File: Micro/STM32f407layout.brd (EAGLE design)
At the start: 100 x 80 mm, 44 parts, among them Q1 ASF, T3 FDN340P, T4 AP1117_LIN_REG

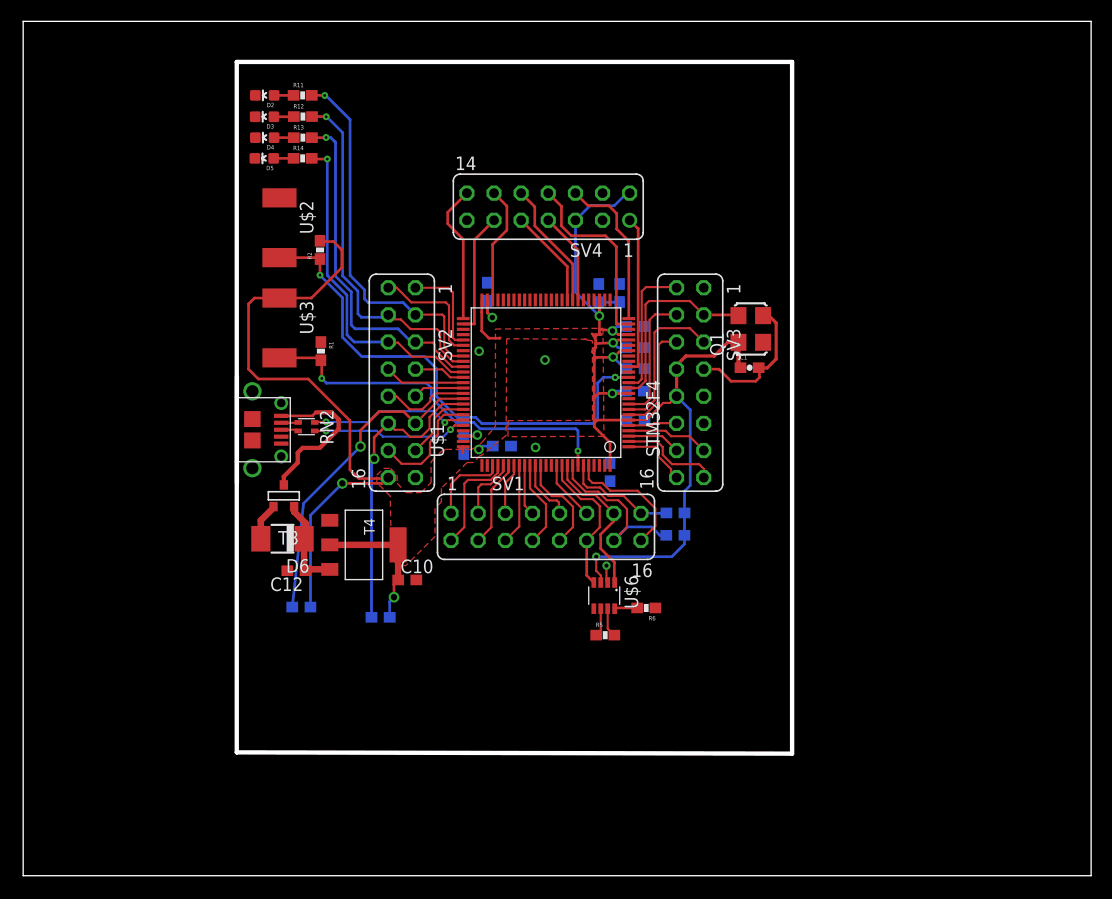
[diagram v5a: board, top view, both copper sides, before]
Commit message: Holiday Update 1
Connected extra capacitors, changed PC0 to GND for now, May route to
better pinout later. Added GND planes made sure no unrouted
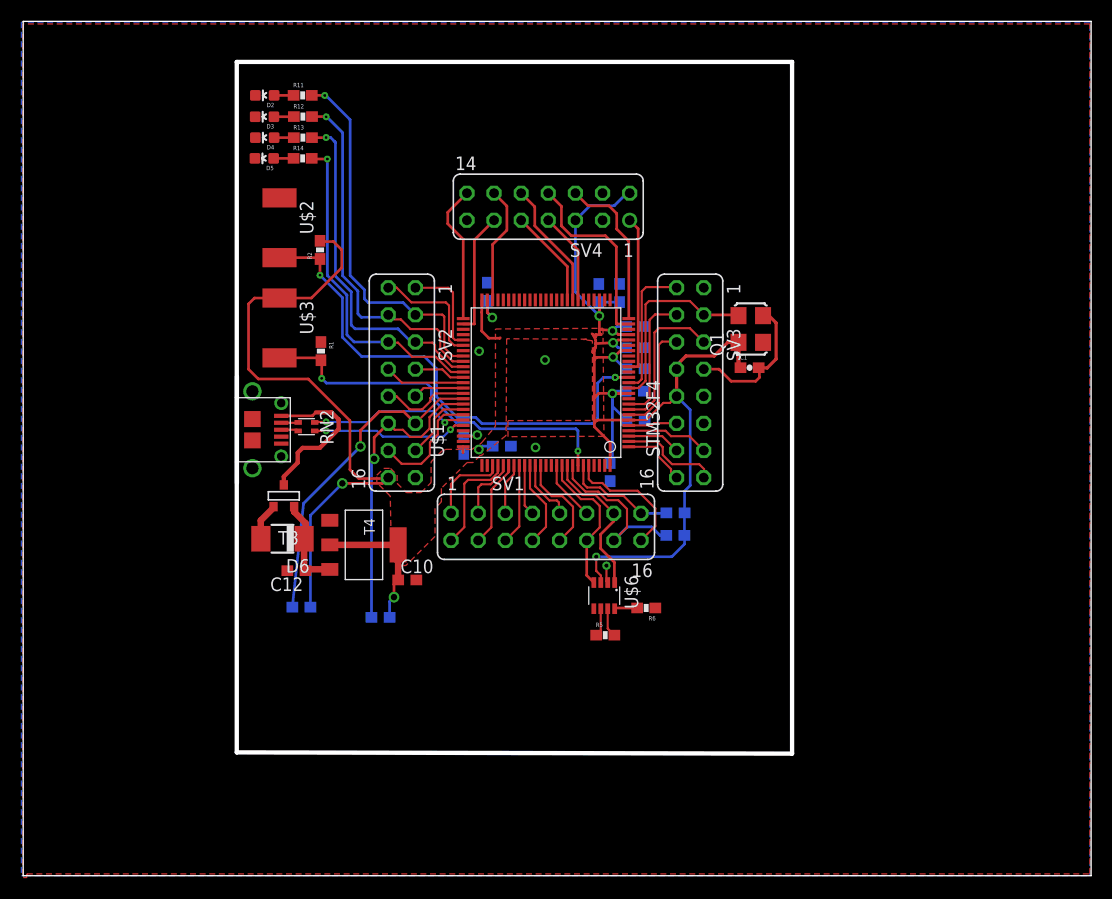
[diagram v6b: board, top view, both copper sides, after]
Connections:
- net GND: now also SV3.1
- net PC0: no longer SV3.1
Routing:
- net +3V3: track 184.5 -> 194.2 mm
- added copper zone on layer 1, net GND
- added copper zone on layer 16, net GND
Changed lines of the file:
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@@
 <layer number="27" name="tValues" color="7" fill="1" visible="yes" active="yes"/>
 <layer number="28" name="bValues" color="7" fill="1" visible="yes" active="yes"/>
-<layer number="29" name="tStop" color="7" fill="3" visible="no" active="yes"/>
-<layer number="30" name="bStop" color="7" fill="6" visible="no" active="yes"/>
+<layer number="29" name="tStop" color="7" fill="3" visible="yes" active="yes"/>
+<layer number="30" name="bStop" color="7" fill="6" visible="yes" active="yes"/>
 <layer number="31" name="tCream" color="7" fill="4" visible="no" active="yes"/>
 <layer number="32" name="bCream" color="7" fill="5" visible="no" active="yes"/>
-<layer number="33" name="tFinish" color="6" fill="3" visible="no" active="yes"/>
-<layer number="34" name="bFinish" color="6" fill="6" visible="no" active="yes"/>
+<layer number="33" name="tFinish" color="6" fill="3" visible="yes" active="yes"/>
+<layer number="34" name="bFinish" color="6" fill="6" visible="yes" active="yes"/>
 <layer number="35" name="tGlue" color="7" fill="4" visible="no" active="yes"/>
 <layer number="36" name="bGlue" color="7" fill="5" visible="no" active="yes"/>
-<layer number="37" name="tTest" color="7" fill="1" visible="no" active="yes"/>
-<layer number="38" name="bTest" color="7" fill="1" visible="no" active="yes"/>
+<layer number="37" name="tTest" color="7" fill="1" visible="yes" active="yes"/>
+<layer number="38" name="bTest" color="7" fill="1" visible="yes" active="yes"/>
 <layer number="39" name="tKeepout" color="4" fill="11" visible="yes" active="yes"/>
 <layer number="40" name="bKeepout" color="1" fill="11" visible="yes" active="yes"/>
@@
 <layer number="42" name="bRestrict" color="1" fill="10" visible="yes" active="yes"/>
 <layer number="43" name="vRestrict" color="2" fill="10" visible="yes" active="yes"/>
-<layer number="44" name="Drills" color="7" fill="1" visible="no" active="yes"/>
-<layer number="45" name="Holes" color="7" fill="1" visible="no" active="yes"/>
-<layer number="46" name="Milling" color="3" fill="1" visible="no" active="yes"/>
-<layer number="47" name="Measures" color="7" fill="1" visible="no" active="yes"/>
+<layer number="44" name="Drills" color="7" fill="1" visible="yes" active="yes"/>
+<layer number="45" name="Holes" color="7" fill="1" visible="yes" active="yes"/>
+<layer number="46" name="Milling" color="3" fill="1" visible="yes" active="yes"/>
+<layer number="47" name="Measures" color="7" fill="1" visible="yes" active="yes"/>
 <layer number="48" name="Document" color="7" fill="1" visible="yes" active="yes"/>
 <layer number="49" name="Reference" color="7" fill="1" visible="yes" active="yes"/>
@@
 <contactref element="SV4" pad="3"/>
 <contactref element="SV4" pad="4"/>
-<wire x1="54.2501375" y1="61.373125" x2="54.2501375" y2="63.913125" width="0" layer="19" extent="1-1"/>
-<wire x1="53.8994875" y1="55.405290625" x2="54.2501375" y2="61.373125" width="0" layer="19" extent="16-16"/>
-<wire x1="54.457" y1="53.915" x2="53.8994875" y2="55.405290625" width="0" layer="19" extent="1-16"/>
-<wire x1="55.845025" y1="55.412146875" x2="53.8994875" y2="55.405290625" width="0" layer="19" extent="16-16"/>
-<wire x1="58.162153125" y1="51.4214625" x2="54.457" y2="53.915" width="0" layer="19" extent="1-16"/>
-<wire x1="58.15608125" y1="49.43988125" x2="58.162153125" y2="51.4214625" width="0" layer="19" extent="16-16"/>
+<polygon width="0.4064" layer="16">
+<vertex x="0.170153125" y="0"/>
+<vertex x="99.885346875" y="0"/>
+<vertex x="99.885346875" y="79.928821875"/>
+<vertex x="-0.170153125" y="79.928821875"/>
+<vertex x="-0.170153125" y="0"/>
+</polygon>
+<polygon width="0.4064" layer="1">
+<vertex x="0.340334375" y="0.170434375"/>
+<vertex x="99.885346875" y="0.170434375"/>
+<vertex x="99.885346875" y="79.7583875"/>
+<vertex x="0" y="79.7583875"/>
+<vertex x="0" y="-0.170434375"/>
+<vertex x="0.340334375" y="-0.170434375"/>
+</polygon>
+<contactref element="SV3" pad="1"/>
+<wire x1="53.8994875" y1="55.405290625" x2="54.457" y2="53.915" width="0" layer="19" extent="1-16"/>
+<wire x1="41.207" y1="40.665" x2="41.26053125" y2="39.49798125" width="0" layer="19" extent="1-16"/>
 <wire x1="56.707" y1="49.665" x2="58.15608125" y2="49.43988125" width="0" layer="19" extent="1-16"/>
-<wire x1="58.185671875" y1="47.4711" x2="58.15608125" y2="49.43988125" width="0" layer="19" extent="16-16"/>
-<wire x1="58.122509375" y1="45.375653125" x2="58.185671875" y2="47.4711" width="0" layer="19" extent="16-16"/>
+<wire x1="54.457" y1="38.415" x2="54.9599625" y2="36.9452" width="0" layer="19" extent="1-16"/>
 <wire x1="56.707" y1="44.665" x2="58.122509375" y2="45.375653125" width="0" layer="19" extent="1-16"/>
-<wire x1="58.187578125" y1="42.6469875" x2="56.707" y2="44.665" width="0" layer="19" extent="1-16"/>
-<wire x1="63.727" y1="47.435" x2="58.185671875" y2="47.4711" width="0" layer="19" extent="16-16"/>
-<wire x1="63.727" y1="44.895" x2="63.727" y2="47.435" width="0" layer="19" extent="1-1"/>
-<wire x1="63.727" y1="42.355" x2="63.727" y2="44.895" width="0" layer="19" extent="1-1"/>
-<wire x1="54.457" y1="38.415" x2="58.187578125" y2="42.6469875" width="0" layer="19" extent="1-16"/>
-<wire x1="54.9599625" y1="36.9452" x2="54.457" y2="38.415" width="0" layer="19" extent="1-16"/>
-<wire x1="54.617896875" y1="29.033775" x2="54.9599625" y2="36.9452" width="0" layer="19" extent="16-16"/>
-<wire x1="59.190259375" y1="25.071378125" x2="54.73334375" y2="27.45334375" width="0" layer="19" extent="1-1"/>
-<wire x1="45.670234375" y1="40.22925625" x2="54.457" y2="38.415" width="0" layer="19" extent="1-16"/>
-<wire x1="41.26053125" y1="39.49798125" x2="45.670234375" y2="40.22925625" width="0" layer="19" extent="16-16"/>
-<wire x1="41.207" y1="40.665" x2="41.26053125" y2="39.49798125" width="0" layer="19" extent="1-16"/>
-<wire x1="36.727" y1="37.275" x2="41.26053125" y2="39.49798125" width="0" layer="19" extent="16-16"/>
-<wire x1="28.709846875" y1="33.280178125" x2="36.727" y2="37.275" width="0" layer="19" extent="1-1"/>
-<wire x1="24.732859375" y1="28.563709375" x2="28.709846875" y2="33.280178125" width="0" layer="19" extent="1-1"/>
-<wire x1="24.16348125" y1="39.2603" x2="28.709846875" y2="33.280178125" width="0" layer="19" extent="1-1"/>
-<wire x1="24.16348125" y1="40.4603" x2="24.16348125" y2="39.2603" width="0" layer="19" extent="1-1"/>
-<wire x1="24.16348125" y1="41.1103" x2="24.16348125" y2="40.4603" width="0" layer="19" extent="1-1"/>
-<wire x1="21.46348125" y1="40.7603" x2="24.16348125" y2="40.4603" width="0" layer="19" extent="1-1"/>
-<wire x1="21.46348125" y1="42.7603" x2="21.46348125" y2="40.7603" width="0" layer="19" extent="1-1"/>
-<wire x1="21.46348125" y1="45.3578" x2="21.46348125" y2="42.7603" width="0" layer="19" extent="1-1"/>
-<wire x1="21.46348125" y1="38.1628" x2="21.46348125" y2="40.7603" width="0" layer="19" extent="1-1"/>
-<wire x1="24.16348125" y1="44.2603" x2="21.46348125" y2="45.3578" width="0" layer="19" extent="1-1"/>
-<wire x1="27.88" y1="49.970890625" x2="24.16348125" y2="44.2603" width="0" layer="19" extent="1-1"/>
-<wire x1="36.8149" y1="27.694153125" x2="36.727" y2="37.275" width="0" layer="19" extent="1-1"/>
-<wire x1="43.464428125" y1="55.524046875" x2="53.8994875" y2="55.405290625" width="0" layer="19" extent="16-16"/>
-<wire x1="24" y1="63.47526875" x2="27.88" y2="49.970890625" width="0" layer="19" extent="1-1"/>
-<wire x1="21.699075" y1="67.169690625" x2="24" y2="63.47526875" width="0" layer="19" extent="1-1"/>
-<wire x1="21.74304375" y1="69.112259375" x2="21.699075" y2="67.169690625" width="0" layer="19" extent="1-1"/>
-<wire x1="21.72458125" y1="71.069228125" x2="21.74304375" y2="69.112259375" width="0" layer="19" extent="1-1"/>
-<wire x1="21.742459375" y1="73.067596875" x2="21.72458125" y2="71.069228125" width="0" layer="19" extent="1-1"/>
 </signal>
 <signal name="+3V3">
@@
 <wire x1="29.888003125" y1="36.73599375" x2="33.64799375" y2="36.73599375" width="0.254" layer="1"/>
 <wire x1="33.64799375" y1="36.73599375" x2="34.187" y2="37.275" width="0.254" layer="1"/>
-<wire x1="56.707" y1="42.665" x2="56.487578125" y2="42.6469875" width="0" layer="19" extent="1-16"/>
-<wire x1="54.9599625" y1="38.6452" x2="54.957" y2="38.415" width="0" layer="19" extent="1-16"/>
+<wire x1="56.487578125" y1="42.6469875" x2="55.16989375" y2="43.964671875" width="0.254" layer="16"/>
+<wire x1="55.16989375" y1="43.964671875" x2="55.16989375" y2="45.15363125" width="0.254" layer="16"/>
+<wire x1="54.9599625" y1="38.6452" x2="55.16989375" y2="38.85513125" width="0.254" layer="16"/>
+<wire x1="55.16989375" y1="38.85513125" x2="55.16989375" y2="45.15363125" width="0.254" layer="16"/>
 </signal>
 <signal name="N$3">
@@
 <signal name="PC0">
 <contactref element="U$1" pad="P15"/>
-<contactref element="SV3" pad="1"/>
-<wire x1="56.707" y1="47.165" x2="63.727" y2="55.055" width="0" layer="19" extent="1-1"/>
 </signal>
 <signal name="PC2">

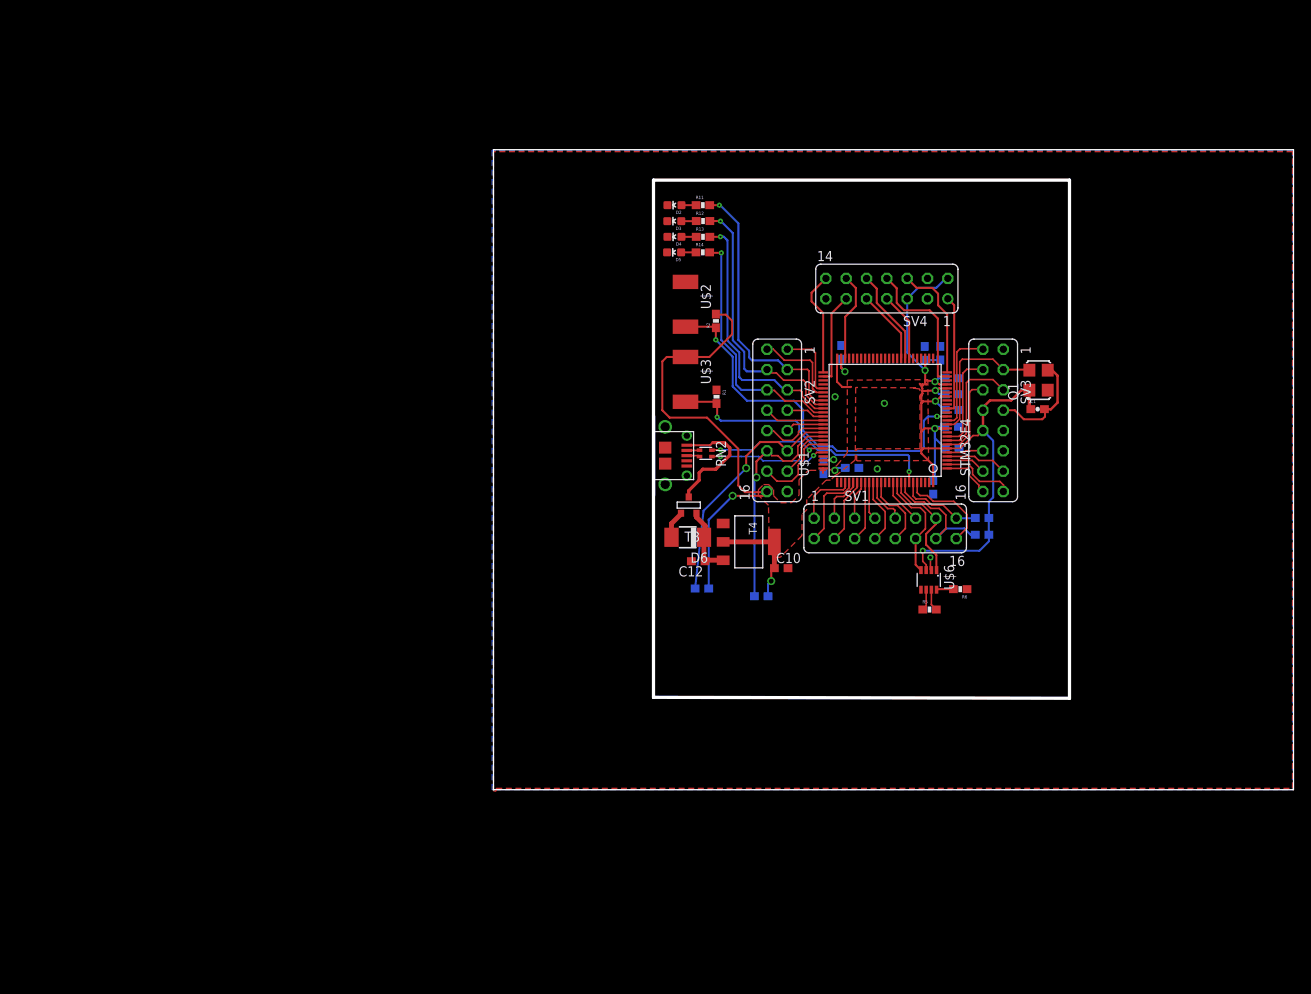
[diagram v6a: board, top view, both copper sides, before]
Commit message: Ethernet Addition
I added the ethernet chip and added essential routes, need to do
tolerance checks
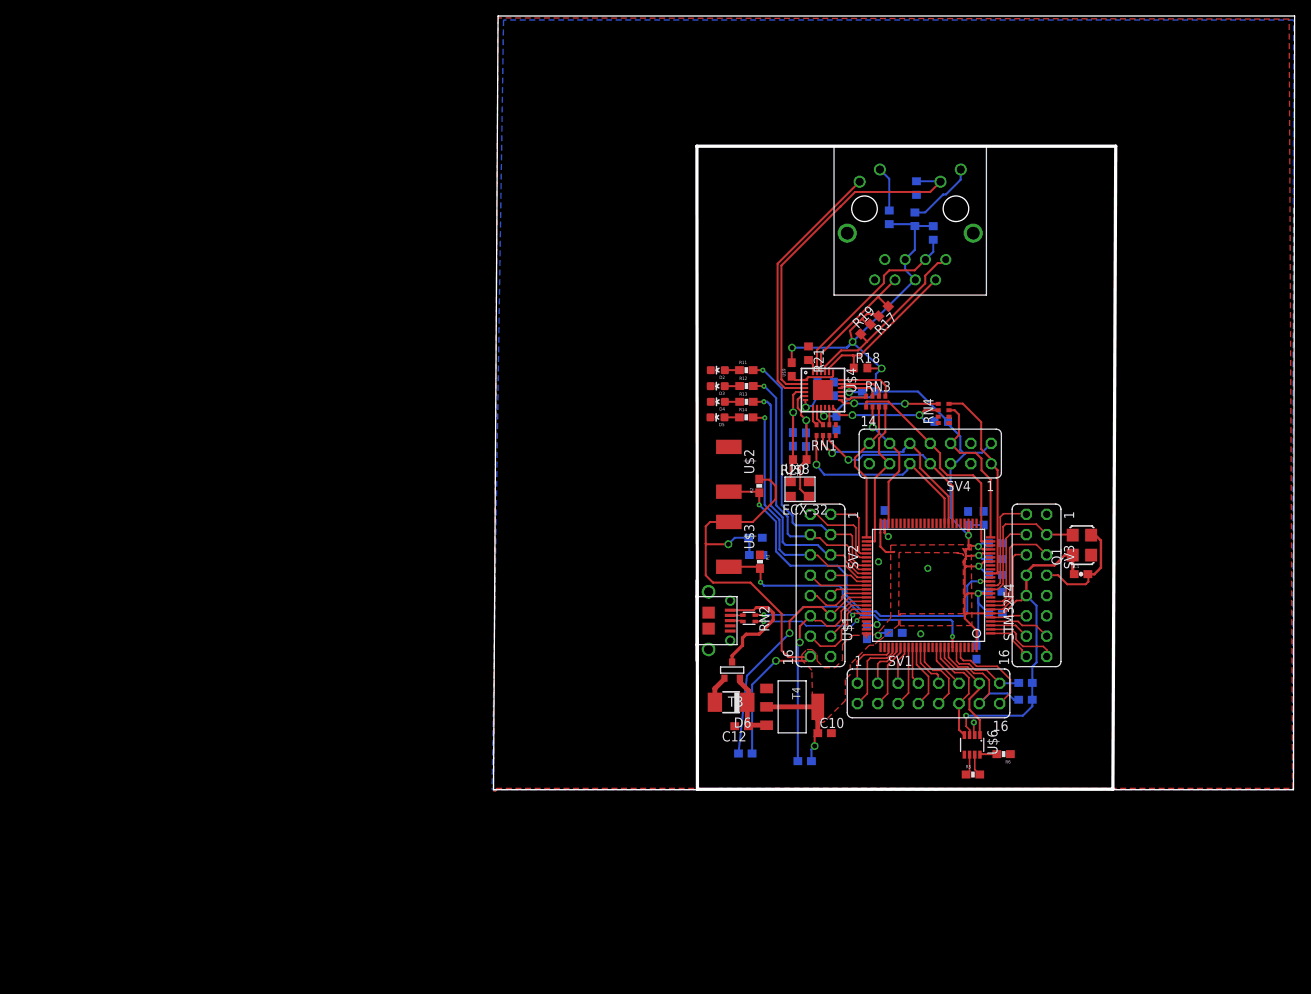
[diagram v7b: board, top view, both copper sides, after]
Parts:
- added C15: 1uF, eagle-ltspice:C0603
- added C16: 1nF, eagle-ltspice:C0603
- added C19, C20, C21: 100nF, eagle-ltspice:C0603
- added C5, C7: 22pF, eagle-ltspice:C0603
- added R15, R7: 250R, resistor:R0603
- added R16, R17, R18, R19: 49.9R, resistor:R0603
- added R20: 1M, resistor:R0603
- added R21: 12.1K, resistor:R0603
- added R22: 4.7K, resistor:R0603
- added R23: 1.5k, resistor:R0603
- added R8: 10K, SparkFun-Passives:0603-RES
- added RN1, RN3, RN4: (no value), resistor-dil:CAY16
- added U$4: LAN8720LAN8720, EthernetChip:24-QFN
- added U$7: J00-0065NL, EthernetChip:J00-0065NL
- added U$8: ECX-32, Other:ECX-32
- added U$9: (no value), EthernetChip:0603
- moved D2 21.3 mm to (28.0, 52.4)
- moved C1 21.3 mm to (73.4, 26.9)
- moved C10 21.3 mm to (41.4, 7.07)
- moved C11 21.3 mm to (62.8, 26.8)
- moved C12 21.3 mm to (31.0, 7.94)
- moved C13 21.3 mm to (50.2, 19.6)
- moved C14 21.3 mm to (60.4, 17.2)
- moved C18 21.3 mm to (62.8, 22.0)
- moved C3 21.3 mm to (48.9, 34.1)
- moved C4 21.3 mm to (59.3, 33.9)
- moved C6 21.3 mm to (62.7, 24.8)
- moved C8 21.3 mm to (61.3, 33.9)
- moved C9 21.3 mm to (62.7, 28.8)
- moved D5 21.3 mm to (28.0, 46.5)
- moved D6 21.3 mm to (29.7, 10.9)
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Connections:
- new net BUS_SPEED: R22.2, U$4.2, U$7.10
- new net GREEN: R7.2, U$7.9
- new net LINK/ACT: U$4.3, U$7.12
- new net MDE: RN4.1, U$4.13
- new net N$13: RN3.4, U$4.14
- new net N$16: RN3.3, U$4.16
- new net N$19: RN3.2, U$4.17
- new net N$20: RN3.1, U$4.18
- new net N$21: U$4.1, U$4.19, U$9.1
- new net N$22: R21.2, U$4.24
- new net N$23: R23.1, RN4.2, U$4.12
- new net N$25: RN1.7, U$4.8
- new net N$26: RN1.8, U$4.7
- new net N$6: C15.2, C16.2, U$4.6
- new net N$9: RN1.6, U$4.11
- new net NRST: R8.1, U$4.15
- new net RD+: R16.1, U$4.23, U$7.3
- new net RD-: R17.1, U$4.22, U$7.6
- new net RXERR: U$4.10
- new net TD+: R19.1, U$4.21, U$7.1
- new net TD-: R18.1, U$4.20, U$7.2
- new net XTAL1: C7.1, R20.1, U$4.5, U$8.OUT/IN
- new net XTAL2: C5.1, R20.2, U$4.4, U$8.IN/OUT
- new net YELLOW: R15.2, U$7.11
- net +3V3: now also C19.2, C20.2, C21.2, R15.1, R16.2, R17.2, R18.2, R19.2, R23.2, R7.1, R8.2, U$4.9, U$7.4, U$7.5, U$9.2
- net CRS_DV: now also RN1.3
- net GND: now also C15.1, C16.1, C19.1, C20.1, C21.1, C5.2, C7.2, R21.1, R22.1, U$4.VSS_PAD, U$7.15, U$7.16, U$7.8, U$8.GND, U$8.GND2
- net MDC: now also RN4.8
- net MDIO: now also RN4.7
- net REFCLK: now also RN3.5
- net RXD0: now also RN1.2
- net RXD1: now also RN1.1
- net TXD0: now also RN3.7
- net TXD1: now also RN3.8
- net TXEN: now also RN3.6
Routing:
- net +3V3: track 194.2 -> 279.3 mm, vias 9 -> 14
- net BUS_SPEED: track 0.00 -> 44.7 mm
- net LINK/ACT: track 0.00 -> 33.0 mm
- net RD+: track 0.00 -> 24.5 mm
- net TD+: track 0.00 -> 23.2 mm
- net TD-: track 0.00 -> 20.1 mm
- net RD-: track 0.00 -> 17.2 mm
- net RXD1: track 9.25 -> 26.0 mm, vias 0 -> 1
- net XTAL1: track 0.00 -> 16.3 mm, vias 0 -> 1
- net N$23: track 0.00 -> 16.0 mm, vias 0 -> 2
- net XTAL2: track 0.00 -> 15.2 mm, vias 0 -> 1
- net CRS_DV: track 8.61 -> 23.7 mm, vias 0 -> 1
- net RXD0: track 12.0 -> 25.1 mm, vias 0 -> 1
- net MDE: track 0.00 -> 12.4 mm, vias 0 -> 2
- net REFCLK: track 17.9 -> 28.7 mm
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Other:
- board size 100 x 80 mm -> 100.1 x 96.7 mm
